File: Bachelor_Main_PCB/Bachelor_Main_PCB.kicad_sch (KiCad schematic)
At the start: 4 parts

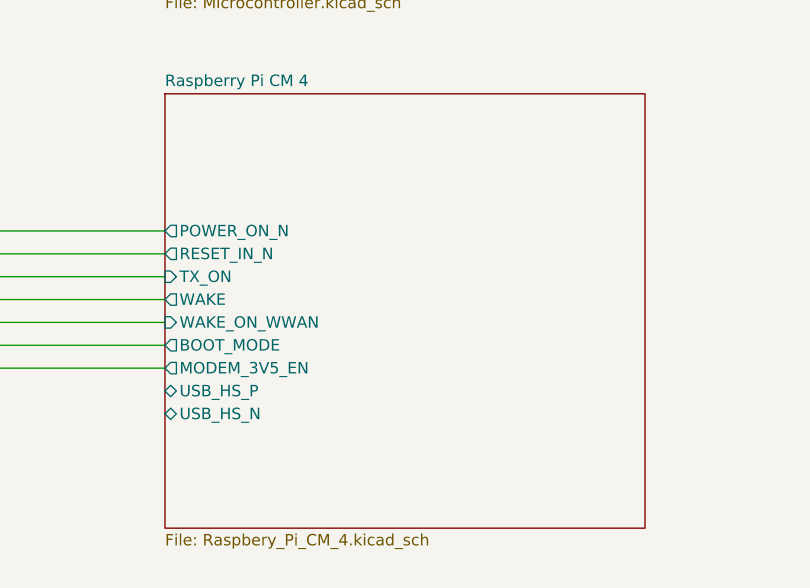
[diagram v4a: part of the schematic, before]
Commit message: Add Vcc to Y1
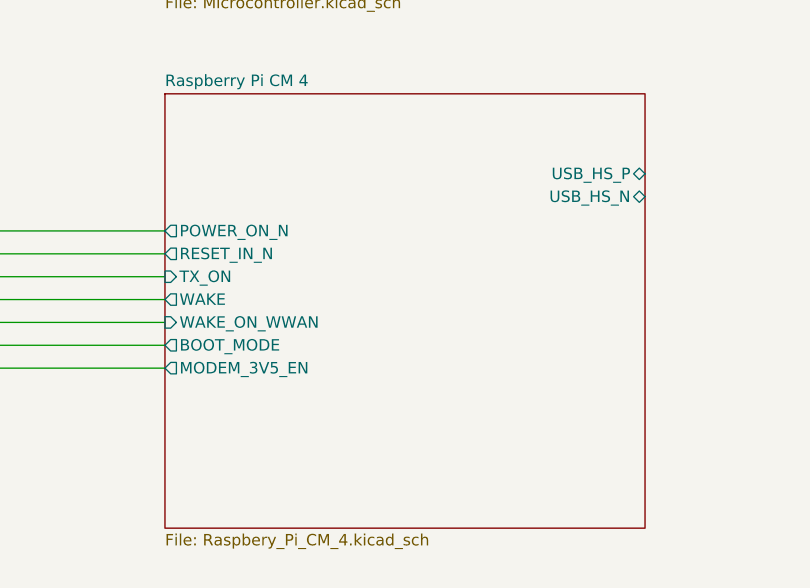
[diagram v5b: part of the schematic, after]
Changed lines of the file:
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@@
 		)
 		(pin "USB_HS_N" bidirectional
-			(at 121.92 134.62 180)
+			(at 175.26 110.49 0)
 			(effects
 				(font
 					(size 1.27 1.27)
 				)
-				(justify left)
+				(justify right)
 			)
 		)
 		(pin "USB_HS_P" bidirectional
-			(at 121.92 132.08 180)
+			(at 175.26 107.95 0)
 			(effects
 				(font
 					(size 1.27 1.27)
 				)
-				(justify left)
+				(justify right)
 			)
 		)

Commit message: Fix hierarchal sheet naming for USB hub
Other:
- sheet Raspberry Pi CM 4 ports: added nEXTRST; removed none
- sheet USB Hub ports: added USB_HUB_IN_M, USB_HUB_IN_P, USB_HUB_OUT_1_M, USB_HUB_OUT_1_P, USB_HUB_OUT_2_M, USB_HUB_OUT_2_P, nEXTRST; removed none
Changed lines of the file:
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@@
+	(wire
+		(pts
+			(xy 175.26 107.95) (xy 190.5 107.95)
+		)
+		(stroke
+			(width 0)
+			(type default)
+		)
+	)
+	(wire
+		(pts
+			(xy 175.26 110.49) (xy 190.5 110.49)
+		)
+		(stroke
+			(width 0)
+			(type default)
+		)
+	)
 	(wire
 		(pts
@@
 		(pts
 			(xy 80.01 114.3) (xy 121.92 114.3)
+		)
+		(stroke
+			(width 0)
+			(type default)
+		)
+	)
+	(wire
+		(pts
+			(xy 175.26 114.3) (xy 190.5 114.3)
 		)
 		(stroke
@@
 			)
 		)
+		(pin "nEXTRST" output
+			(at 175.26 114.3 0)
+			(effects
+				(font
+					(size 1.27 1.27)
+				)
+				(justify right)
+			)
+		)
 		(instances
 			(project "Bachelor_Main_PCB"
@@
 	)
 	(sheet
-		(at 200.66 83.82)
+		(at 190.5 87.63)
 		(size 45.72 27.94)
 		(exclude_from_sim no)
@@
 		)
 		(property "Sheetname" "USB Hub"
-			(at 200.66 83.1084 0)
+			(at 190.5 86.9184 0)
 			(effects
 				(font
@@
 		)
 		(property "Sheetfile" "USB_HUB.kicad_sch"
-			(at 200.66 112.3446 0)
+			(at 190.5 116.1546 0)
 			(effects
 				(font
@@
 			)
 		)
+		(pin "nEXTRST" input
+			(at 190.5 114.3 180)
+			(effects
+				(font
+					(size 1.27 1.27)
+				)
+				(justify left)
+			)
+		)
+		(pin "USB_HUB_IN_M" bidirectional
+			(at 190.5 110.49 180)
+			(effects
+				(font
+					(size 1.27 1.27)
+				)
+				(justify left)
+			)
+		)
+		(pin "USB_HUB_IN_P" bidirectional
+			(at 190.5 107.95 180)
+			(effects
+				(font
+					(size 1.27 1.27)
+				)
+				(justify left)
+			)
+		)
+		(pin "USB_HUB_OUT_1_M" bidirectional
+			(at 190.5 90.17 180)
+			(effects
+				(font
+					(size 1.27 1.27)
+				)
+				(justify left)
+			)
+		)
+		(pin "USB_HUB_OUT_1_P" bidirectional
+			(at 190.5 92.71 180)
+			(effects
+				(font
+					(size 1.27 1.27)
+				)
+				(justify left)
+			)
+		)
+		(pin "USB_HUB_OUT_2_M" bidirectional
+			(at 190.5 96.52 180)
+			(effects
+				(font
+					(size 1.27 1.27)
+				)
+				(justify left)
+			)
+		)
+		(pin "USB_HUB_OUT_2_P" bidirectional
+			(at 190.5 99.06 180)
+			(effects
+				(font
+					(size 1.27 1.27)
+				)
+				(justify left)
+			)
+		)

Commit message: Routed Sheeets
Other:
- sheet USB Hub ports: added USB_HUB_IN_N, USB_HUB_OUT_1_N, USB_HUB_OUT_2_N; removed USB_HUB_IN_M, USB_HUB_OUT_1_M, USB_HUB_OUT_2_M
- note added: "Power supply lines are not drawn as hierarcical but global lables due to the high amount of them"
- note removed: "Power supply lines are not drawn as hierarcical but global lables"
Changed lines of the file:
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@@
 	(generator_version "9.0")
 	(paper "A4")
-	(text "Power supply lines are not drawn as hierarcical but global lables"
+	(text "Power supply lines are not drawn as hierarcical but global lables\ndue to the high amount of them"
 		(exclude_from_sim no)
-		(at 119.888 156.21 0)
+		(at 120.142 163.576 0)
 		(effects
 			(font
@@
 	(wire
 		(pts
+			(xy 80.01 111.76) (xy 101.6 111.76)
+		)
+		(stroke
+			(width 0)
+			(type default)
+		)
+	)
+	(wire
+		(pts
 			(xy 175.26 110.49) (xy 190.5 110.49)
 		)
@@
 	(wire
 		(pts
-			(xy 83.82 71.12) (xy 121.92 71.12)
+			(xy 182.88 92.71) (xy 182.88 68.58)
+		)
+		(stroke
+			(width 0)
+			(type default)
+		)
+	)
+	(wire
+		(pts
+			(xy 99.06 109.22) (xy 80.01 109.22)
+		)
+		(stroke
+			(width 0)
+			(type default)
+		)
+	)
+	(wire
+		(pts
+			(xy 101.6 111.76) (xy 101.6 99.06)
+		)
+		(stroke
+			(width 0)
+			(type default)
+		)
+	)
+	(wire
+		(pts
+			(xy 182.88 68.58) (xy 148.59 68.58)
+		)
+		(stroke
+			(width 0)
+			(type default)
+		)
+	)
+	(wire
+		(pts
+			(xy 83.82 60.96) (xy 101.6 60.96)
+		)
+		(stroke
+			(width 0)
+			(type default)
+		)
+	)
+	(wire
+		(pts
+			(xy 99.06 96.52) (xy 99.06 109.22)
 		)
 		(stroke
@@
 	(wire
 		(pts
+			(xy 190.5 92.71) (xy 182.88 92.71)
+		)
+		(stroke
+			(width 0)
+			(type default)
+		)
+	)
+	(wire
+		(pts
 			(xy 80.01 127) (xy 121.92 127)
 		)
@@
 	(wire
 		(pts
+			(xy 190.5 96.52) (xy 99.06 96.52)
+		)
+		(stroke
+			(width 0)
+			(type default)
+		)
+	)
+	(wire
+		(pts
+			(xy 185.42 90.17) (xy 185.42 66.04)
+		)
+		(stroke
+			(width 0)
+			(type default)
+		)
+	)
+	(wire
+		(pts
 			(xy 80.01 124.46) (xy 121.92 124.46)
 		)
@@
 	(wire
 		(pts
-			(xy 83.82 106.68) (xy 83.82 71.12)
+			(xy 185.42 66.04) (xy 148.59 66.04)
+		)
+		(stroke
+			(width 0)
+			(type default)
+		)
+	)
+	(wire
+		(pts
+			(xy 83.82 106.68) (xy 83.82 60.96)
+		)
+		(stroke
+			(width 0)
+			(type default)
+		)
+	)
+	(wire
+		(pts
+			(xy 101.6 99.06) (xy 190.5 99.06)
 		)
 		(stroke
@@
 		(pts
 			(xy 80.01 119.38) (xy 121.92 119.38)
+		)
+		(stroke
+			(width 0)
+			(type default)
+		)
+	)
+	(wire
+		(pts
+			(xy 190.5 90.17) (xy 185.42 90.17)
 		)
 		(stroke
@@
 		)
 		(pin "MODEM_USB_DN" bidirectional
+			(at 80.01 111.76 0)
+			(effects
+				(font
+					(size 1.27 1.27)
+				)
+				(justify right)
+			)
+		)
+		(pin "MODEM_USB_DP" bidirectional
 			(at 80.01 109.22 0)
-			(effects
-				(font
-					(size 1.27 1.27)
-				)
-				(justify right)
-			)
-		)
-		(pin "MODEM_USB_DP" bidirectional
-			(at 80.01 111.76 0)
 			(effects
 				(font
@@
 	)
 	(sheet
-		(at 121.92 99.06)
-		(size 53.34 48.26)
+		(at 121.92 105.41)
+		(size 53.34 41.91)
 		(exclude_from_sim no)
 		(in_bom yes)
@@
 		)
 		(property "Sheetname" "Raspberry Pi CM 4"
-			(at 121.92 98.3484 0)
+			(at 121.92 104.6984 0)
 			(effects
 				(font
@@
 	)
 	(sheet
-		(at 97.79 160.02)
-		(size 45.72 24.13)
+		(at 97.79 167.64)
+		(size 45.72 16.51)
 		(exclude_from_sim no)
 		(in_bom yes)
@@
 		)
 		(property "Sheetname" "Power supply"
-			(at 97.79 159.3084 0)
+			(at 97.79 166.9284 0)
 			(effects
 				(font
@@
 	)
 	(sheet
-		(at 121.92 57.15)
+		(at 101.6 46.99)
 		(size 46.99 30.48)
 		(exclude_from_sim no)
@@
 		)
 		(property "Sheetname" "Microcontroller"
-			(at 121.92 56.4384 0)
+			(at 101.6 46.2784 0)
 			(effects
 				(font
@@
 		)
 		(property "Sheetfile" "Microcontroller.kicad_sch"
-			(at 121.92 88.2146 0)
+			(at 101.6 78.0546 0)
 			(effects
 				(font
@@
 		)
 		(pin "RPI_5v" input
-			(at 168.91 69.85 0)
+			(at 148.59 59.69 0)
 			(effects
 				(font
@@
 		)
 		(pin "USB_HS_N" bidirectional
-			(at 168.91 78.74 0)
+			(at 148.59 68.58 0)
 			(effects
 				(font
@@
 		)
 		(pin "USB_HS_P" bidirectional
-			(at 168.91 76.2 0)
+			(at 148.59 66.04 0)
 			(effects
 				(font
@@
 		)
 		(pin "MODEM_SAFE_PWR_REMOVE" output
-			(at 121.92 71.12 180)
+			(at 101.6 60.96 180)
 			(effects
 				(font
@@
 			)
 		)
-		(pin "USB_HUB_IN_M" bidirectional
-			(at 190.5 110.49 180)
-			(effects
-				(font
-					(size 1.27 1.27)
-				)
-				(justify left)
-			)
-		)
 		(pin "USB_HUB_IN_P" bidirectional
 			(at 190.5 107.95 180)
@@
 			)
 		)
-		(pin "USB_HUB_OUT_1_M" bidirectional
+		(pin "USB_HUB_OUT_1_P" bidirectional
 			(at 190.5 90.17 180)
 			(effects
@@
 			)
 		)
-		(pin "USB_HUB_OUT_1_P" bidirectional
+		(pin "USB_HUB_OUT_2_P" bidirectional
+			(at 190.5 96.52 180)
+			(effects
+				(font
+					(size 1.27 1.27)
+				)
+				(justify left)
+			)
+		)
+		(pin "USB_HUB_IN_N" bidirectional
+			(at 190.5 110.49 180)
+			(effects
+				(font
+					(size 1.27 1.27)
+				)
+				(justify left)
+			)
+		)
+		(pin "USB_HUB_OUT_1_N" bidirectional
 			(at 190.5 92.71 180)
 			(effects
@@
 			)
 		)
-		(pin "USB_HUB_OUT_2_M" bidirectional
-			(at 190.5 96.52 180)
-			(effects
-				(font
-					(size 1.27 1.27)
-				)
-				(justify left)
-			)
-		)
-		(pin "USB_HUB_OUT_2_P" bidirectional
+		(pin "USB_HUB_OUT_2_N" bidirectional
 			(at 190.5 99.06 180)
 			(effects

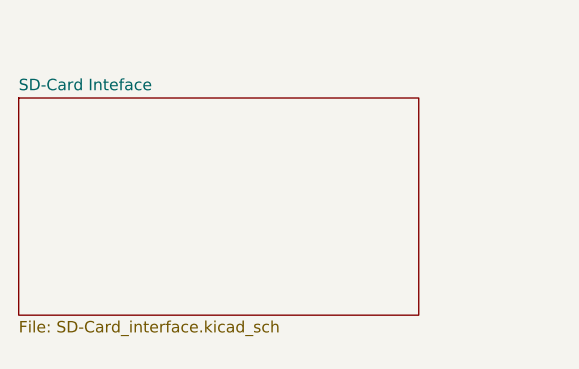
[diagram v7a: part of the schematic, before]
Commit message: Add SD CARD pullups
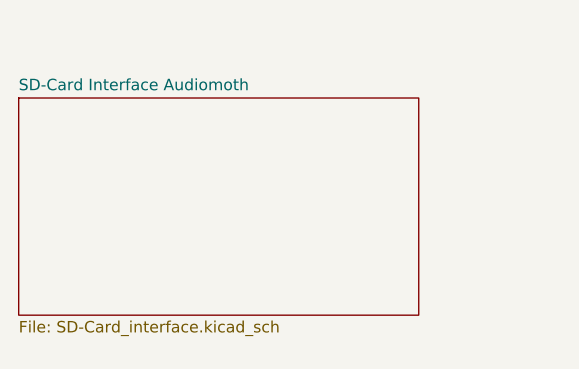
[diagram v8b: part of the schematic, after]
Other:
- sheet SD-Card Inteface renamed SD-Card Interface Audiomoth
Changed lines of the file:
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@@
 			(color 0 0 0 0.0000)
 		)
-		(property "Sheetname" "SD-Card Inteface"
+		(property "Sheetname" "SD-Card Interface Audiomoth"
 			(at 30.48 25.9584 0)
 			(effects
